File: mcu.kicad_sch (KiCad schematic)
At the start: 52 parts, among them J1 Nerdstern, J10 MotorNTC, J12 HallEncoder, J3 Open+Close, J4 SWD, J5 6Pin DuPont 2.56mm, J7 LockState, J8 DoorState, Q1 IRLML0030, SW1 Reset, U1 STM32G0B1KET, U2 24LC64, U5 USBLC6-2SC6, U6 USBLC6-2SC6, Y1 ABM3B-16MHz

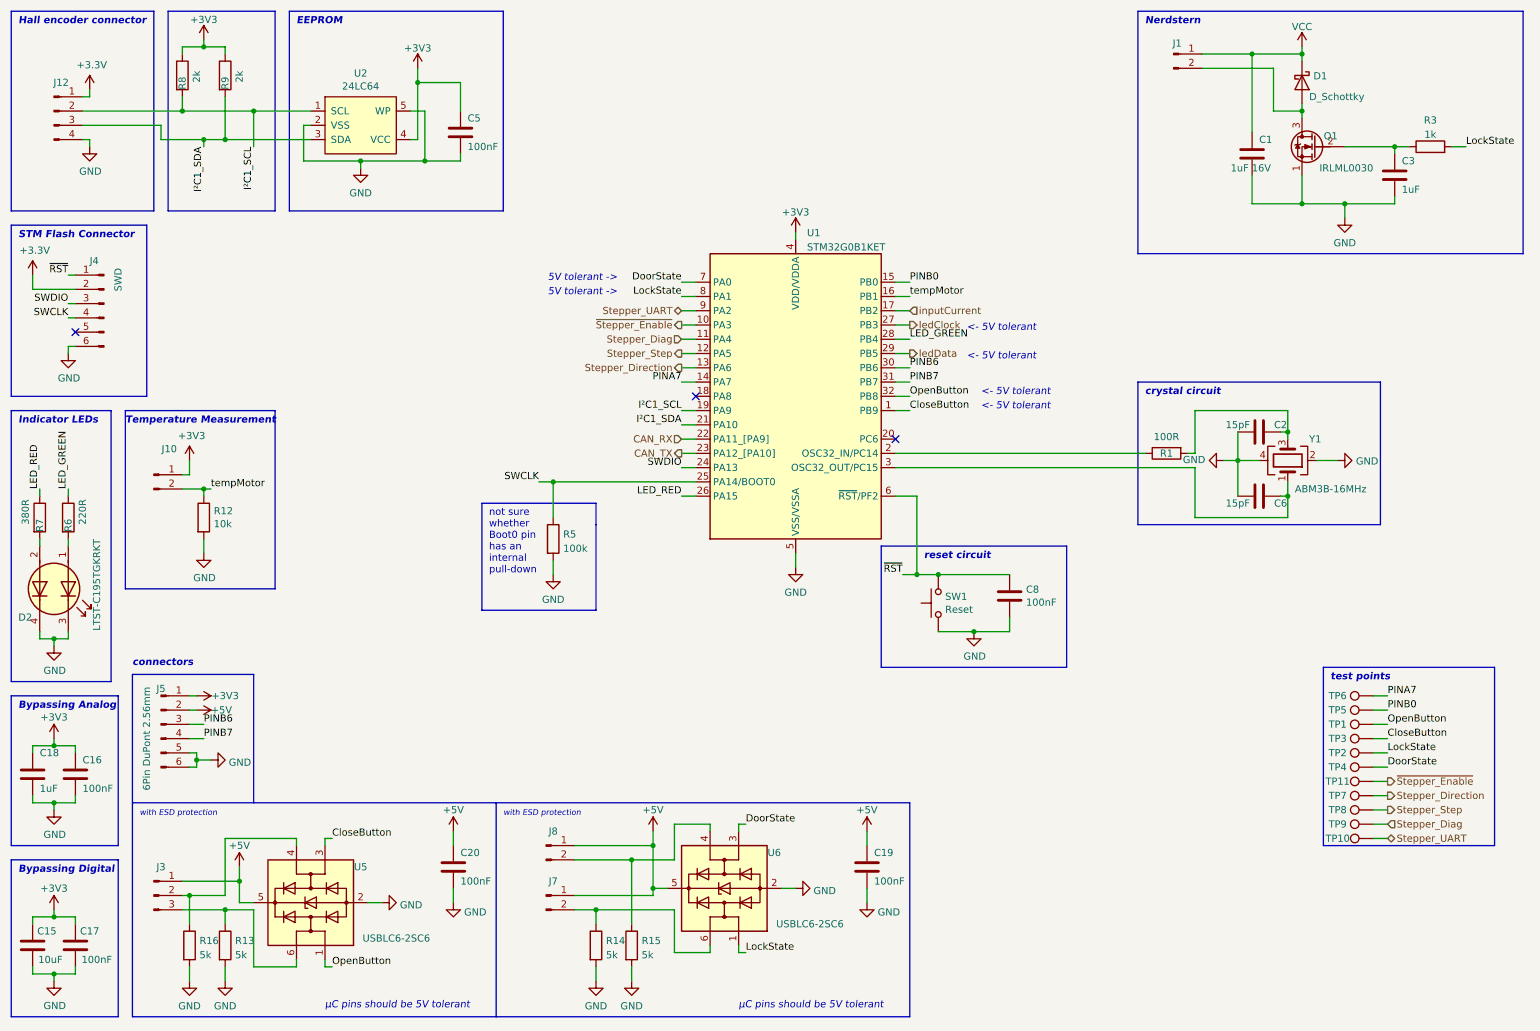
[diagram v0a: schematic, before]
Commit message: Add BOM and update some values due component order
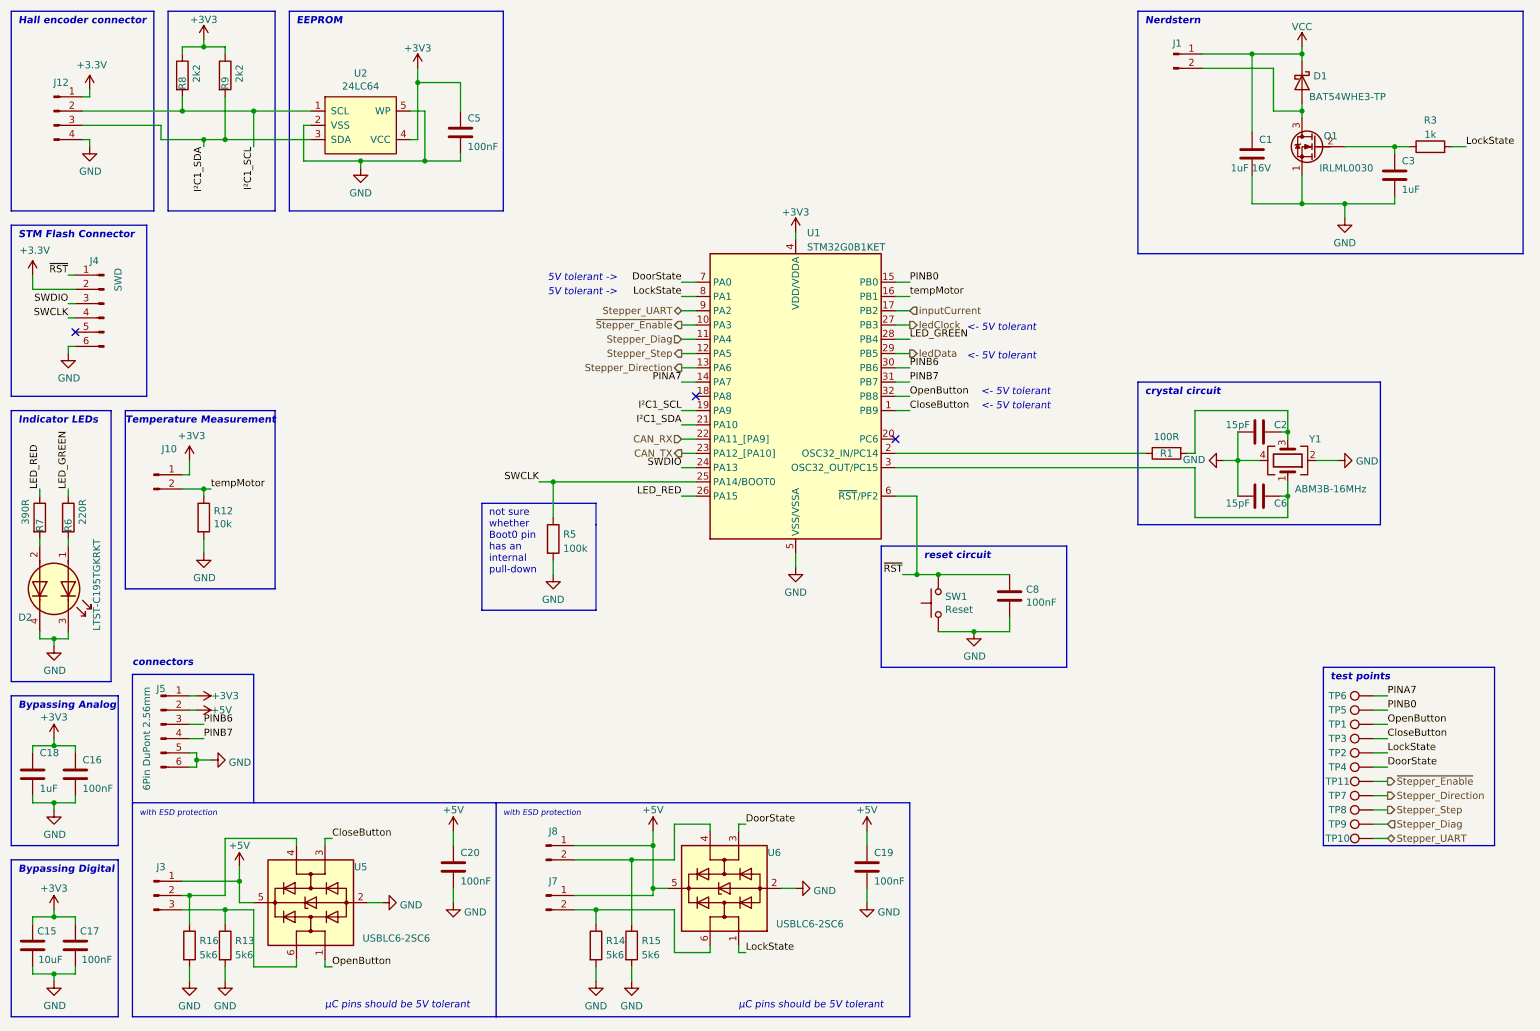
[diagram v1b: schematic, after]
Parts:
- D1: value D_Schottky -> BAT54WHE3-TP; footprint Diode_SMD:D_SOD-523 -> Diode_SMD:D_SOD-123
- R13, R14, R15, R16: value 5k -> 5k6
- R7: value 380R -> 390R
- R8, R9: value 2k -> 2k2
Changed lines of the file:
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@@
       (effects (font (size 1.27 1.27)) (justify left))
     )
-    (property "Value" "380R" (id 1) (at 16.51 105.41 90)
+    (property "Value" "390R" (id 1) (at 16.51 105.41 90)
       (effects (font (size 1.27 1.27)) (justify left))
     )
@@
       (effects (font (size 1.27 1.27)) (justify left))
     )
-    (property "Value" "2k" (id 1) (at 54.61 26.67 90)
+    (property "Value" "2k2" (id 1) (at 54.61 26.67 90)
       (effects (font (size 1.27 1.27)) (justify left))
     )
@@
       (effects (font (size 1.27 1.27)) (justify left))
     )
-    (property "Value" "2k" (id 1) (at 46.99 26.67 90)
+    (property "Value" "2k2" (id 1) (at 46.99 26.67 90)
       (effects (font (size 1.27 1.27)) (justify left))
     )
@@
       (effects (font (size 1.27 1.27)) (justify left))
     )
-    (property "Value" "5k" (id 1) (at 47.498 182.0422 0)
+    (property "Value" "5k6" (id 1) (at 47.498 182.0422 0)
       (effects (font (size 1.27 1.27)) (justify left))
     )
@@
       (effects (font (size 1.27 1.27)) (justify left))
     )
-    (property "Value" "5k" (id 1) (at 53.848 182.0422 0)
+    (property "Value" "5k6" (id 1) (at 53.848 182.0422 0)
       (effects (font (size 1.27 1.27)) (justify left))
     )
@@
       (effects (font (size 1.27 1.27)) (justify left))
     )
-    (property "Value" "D_Schottky" (id 1) (at 245.11 29.21 90)
-      (effects (font (size 1.27 1.27)) (justify left))
-    )
-    (property "Footprint" "Diode_SMD:D_SOD-523" (id 2) (at 243.84 26.67 0)
+    (property "Value" "BAT54WHE3-TP" (id 1) (at 245.11 29.21 90)
+      (effects (font (size 1.27 1.27)) (justify left))
+    )
+    (property "Footprint" "Diode_SMD:D_SOD-123" (id 2) (at 243.84 26.67 0)
       (effects (font (size 1.27 1.27)) hide)
     )
@@
       (effects (font (size 1.27 1.27)) (justify left))
     )
-    (property "Value" "5k" (id 1) (at 126.238 182.0422 0)
+    (property "Value" "5k6" (id 1) (at 126.238 182.0422 0)
       (effects (font (size 1.27 1.27)) (justify left))
     )
@@
       (effects (font (size 1.27 1.27)) (justify left))
     )
-    (property "Value" "5k" (id 1) (at 119.888 182.0422 0)
-      (effects (font (size 1.27 1.27)) (justify left))
-    )
+    (property "Value" "5k6" (id 1) (at 119.888 182.0422 0)
+      (effects (font (size 1.27 1.27)) (justify left))
+    )

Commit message: Change positions of mounting holes to middle
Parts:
- J5: footprint Connector_PinHeader_2.54mm:PinHeader_1x06_P2.54mm_Vertical -> Connector_PinHeader_2.54mm:PinHeader_2x03_P2.54mm_Vertical
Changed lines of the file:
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@@
     (property "Reference" "J5" (id 0) (at 40.64 134.62 0))
     (property "Value" "6Pin DuPont 2.56mm" (id 1) (at 38.1 143.51 90))
-    (property "Footprint" "Connector_PinHeader_2.54mm:PinHeader_1x06_P2.54mm_Vertical" (id 2) (at 40.64 140.97 0)
+    (property "Footprint" "Connector_PinHeader_2.54mm:PinHeader_2x03_P2.54mm_Vertical" (id 2) (at 40.64 140.97 0)
       (effects (font (size 1.27 1.27)) hide)
     )

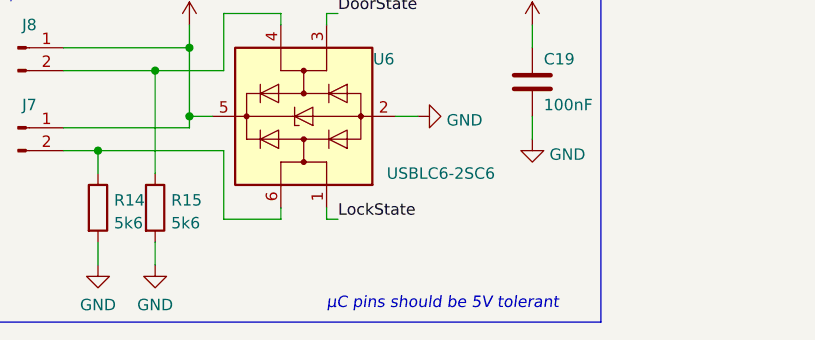
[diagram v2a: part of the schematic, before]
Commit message: Add note to door/lock state switches
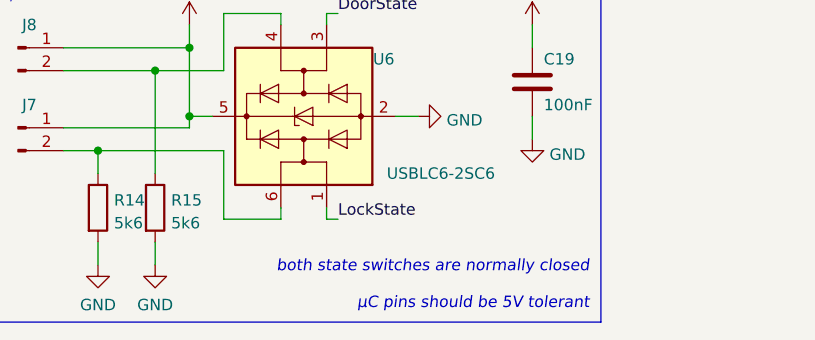
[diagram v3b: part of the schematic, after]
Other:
- note added: "both state switches are normally closed µC pins should be 5V tolerant"
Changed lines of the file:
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@@
     (effects (font (size 1.27 1.27) italic) (justify left bottom))
   )
-  (text "µC pins should be 5V tolerant" (at 143.51 191.77 0)
-    (effects (font (size 1.27 1.27) italic) (justify left bottom))
+  (text "both state switches are normally closed\n\nµC pins should be 5V tolerant"
+    (at 172.72 191.77 0)
+    (effects (font (size 1.27 1.27) italic) (justify right bottom))
   )
   (text "with ESD protection" (at 101.6 157.48 0)

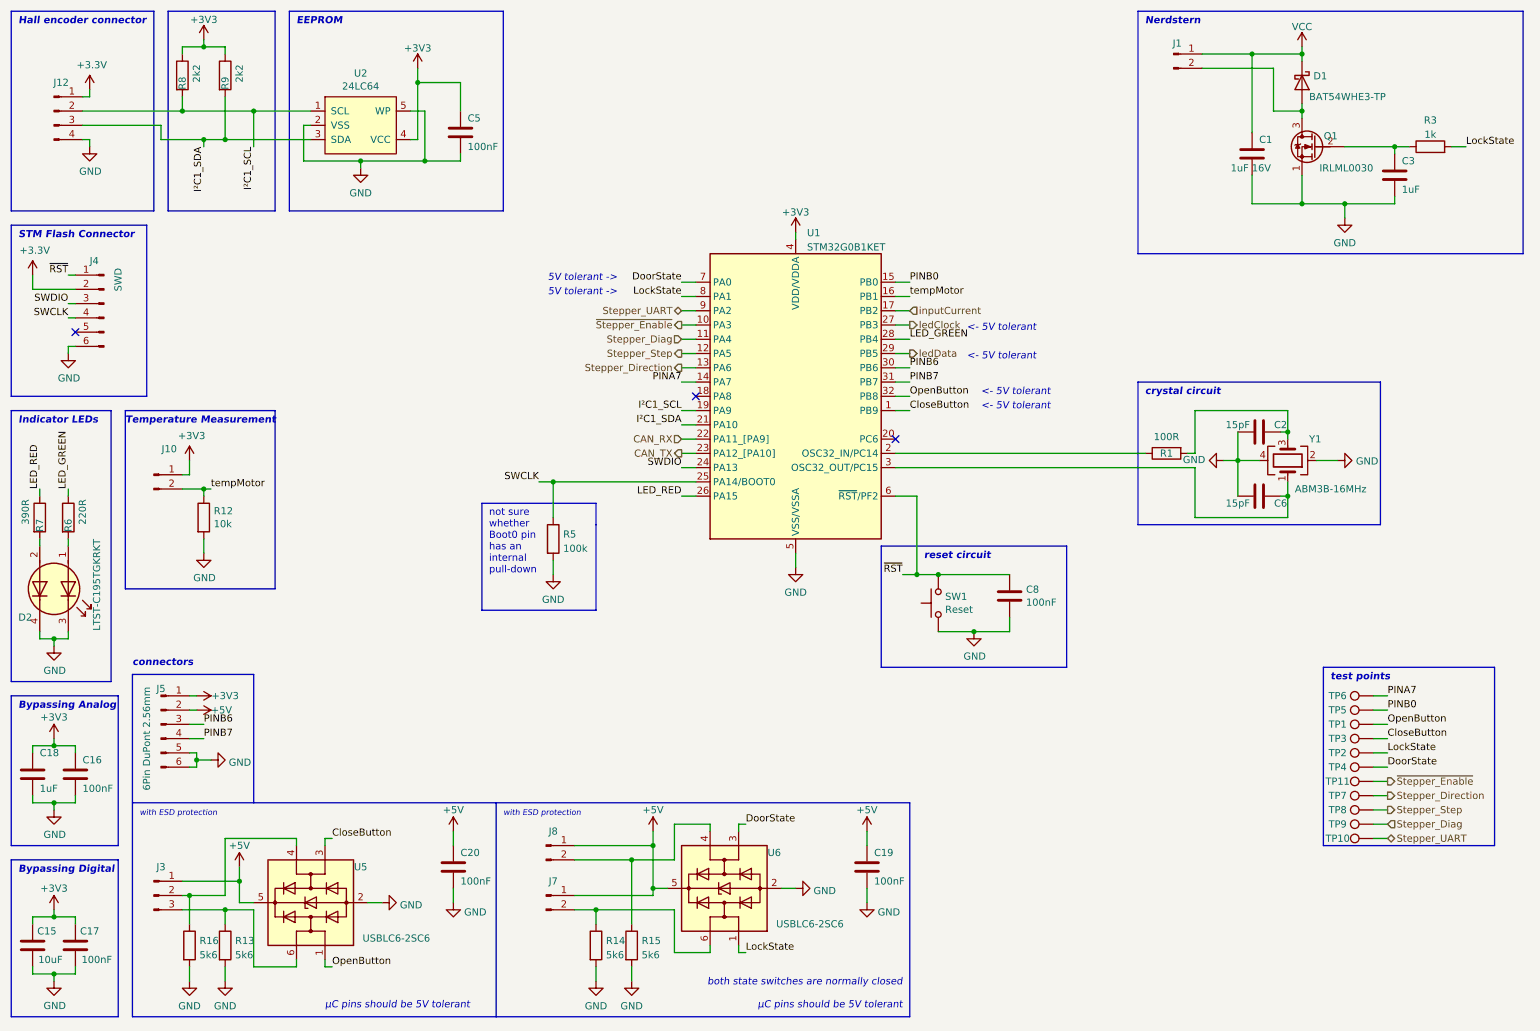
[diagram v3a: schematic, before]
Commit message: Apply suggestions from tux: Single connector for signals Some (better) notes
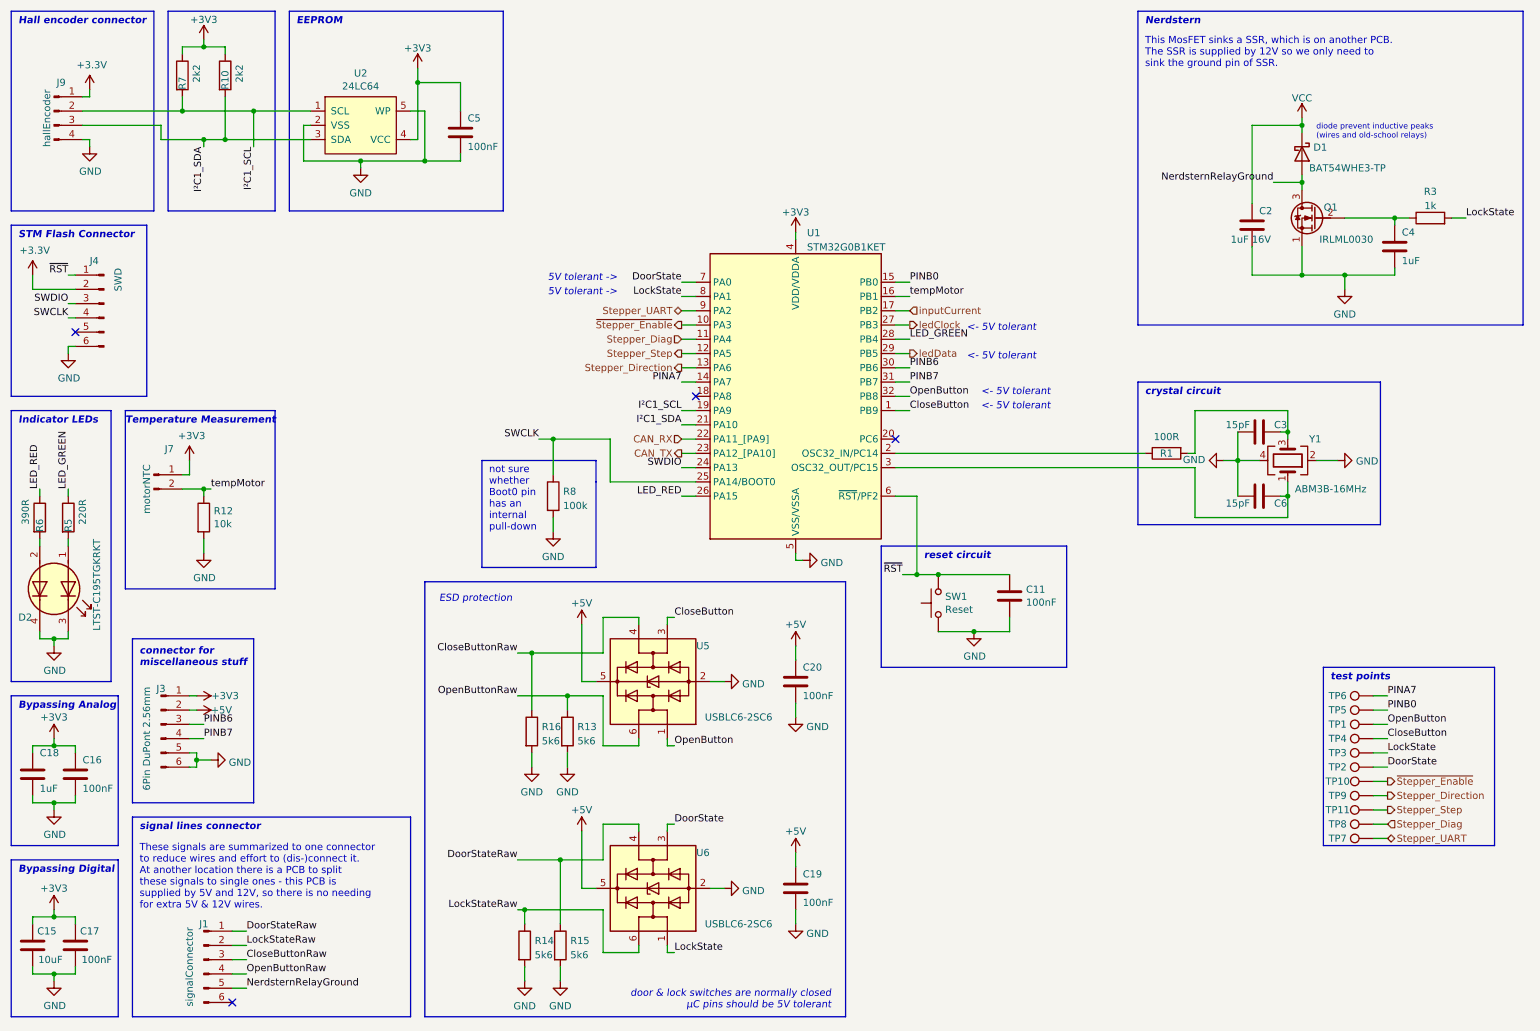
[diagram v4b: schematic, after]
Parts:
- removed J1: Nerdstern, Connector_Molex:Molex_PicoBlade_53047-0210_1x02_P1.25mm_Vertical, symbol Connector:Conn_01x02_Male
- removed J3: Open+Close, Connector_Molex:Molex_PicoBlade_53047-0310_1x03_P1.25mm_Vertical, symbol Connector:Conn_01x03_Male
- removed J7: LockState, Connector_Molex:Molex_PicoBlade_53047-0210_1x02_P1.25mm_Vertical, symbol Connector:Conn_01x02_Male
- removed J8: DoorState, Connector_Molex:Molex_PicoBlade_53047-0210_1x02_P1.25mm_Vertical, symbol Connector:Conn_01x02_Male
- added J1: signalConnector, Connector_Molex:Molex_PicoBlade_53047-0610_1x06_P1.25mm_Vertical, symbol Connector:Conn_01x06_Male
- J7: renamed from J10; value MotorNTC -> motorNTC
- J9: renamed from J12; value HallEncoder -> hallEncoder
- renumbered C8 to C11, C1 to C2, C2 to C3, C3 to C4, J5 to J3, R9 to R10, R6 to R5, R7 to R6, R8 to R7, R5 to R8, TP11 to TP10, TP8 to TP11, TP4 to TP2, TP2 to TP3, TP3 to TP4, TP10 to TP7, TP9 to TP8, TP7 to TP9
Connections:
- net CloseButtonRaw: now reaches R16.1, U5.4 (I/O2)
- net CloseButtonRaw: now also J1.3 (Pin_3)
- net OpenButtonRaw: now reaches R13.1, U5.6 (I/O1)
- net OpenButtonRaw: now also J1.4 (Pin_4)
- net LockStateRaw: now reaches R14.1, U6.6 (I/O1)
- net LockStateRaw: now also J1.2 (Pin_2)
- net NerdsternRelayGround: now reaches D1.2 (A), Q1.3 (D)
- net NerdsternRelayGround: now also J1.5 (Pin_5)
- net DoorStateRaw: now reaches R15.1, U6.4 (I/O2)
- net DoorStateRaw: now also J1.1 (Pin_1)
- no-connect marks 3 -> 4
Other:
- note added: "ESD protection"
- note added: "These signals are summarized to one connector to reduce wires and effort to (dis-)connect it. At another location there is a PCB to split these signals to single ones - this PCB is supplied by 5V and 12V, so there is no needing for extra 5V & 12V wires."
- note added: "This MosFET sinks a SSR, which is on another PCB. The SSR is supplied by 12V so we only need to sink the ground pin of SSR."
- note added: "connector for miscellaneous stuff"
- note added: "diode prevent inductive peaks (wires and old-school relays)"
- note added: "door & lock switches are normally closed µC pins should be 5V tolerant"
- note added: "signal lines connector"
- note removed: "both state switches are normally closed µC pins should be 5V tolerant"
- note removed: "connectors"
- note removed: "with ESD protection"
- note removed: "µC pins should be 5V tolerant"
- moved on the sheet: C19, C2, C20, C4, D1, Q1, R13, R14, R15, R16, R3, R8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

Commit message: Add signal-splitter pcb
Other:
- note added: "These signals are summarized to one connector to reduce wires and effort to (dis-)connect it. At another location there is the signal-splitter PCB to split these signals to single ones. This PCB is supplied by 5V and 12V, so there is no needing for extra 5V & 12V wires."
- note removed: "These signals are summarized to one connector to reduce wires and effort to (dis-)connect it. At another location there is a PCB to split these signals to single ones - this PCB is supplied by 5V and 12V, so there is no needing for extra 5V & 12V wires."
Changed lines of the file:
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@@
     (effects (font (size 1.27 1.27) (thickness 0.254) bold italic) (justify left bottom))
   )
-  (text "These signals are summarized to one connector\nto reduce wires and effort to (dis-)connect it.\nAt another location there is a PCB to split\nthese signals to single ones - this PCB is \nsupplied by 5V and 12V, so there is no needing\nfor extra 5V & 12V wires."
+  (text "These signals are summarized to one connector\nto reduce wires and effort to (dis-)connect it.\nAt another location there is the signal-splitter\nPCB to split these signals to single ones. This\nPCB is supplied by 5V and 12V, so there is no\nneeding for extra 5V & 12V wires."
     (at 36.83 173.99 0)
     (effects (font (size 1.27 1.27)) (justify left bottom))
